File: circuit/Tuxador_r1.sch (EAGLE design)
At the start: 27 parts, among them CN1 MKDSN1,5/2-5,08, CN2 MKDSN1,5/2-5,08, CN3 MKDSN1,5/2-5,08, CN4 MKDSN1,5/2-5,08, IC1 7805T, U1 ATMEGA328P-AU, X1 16MHz

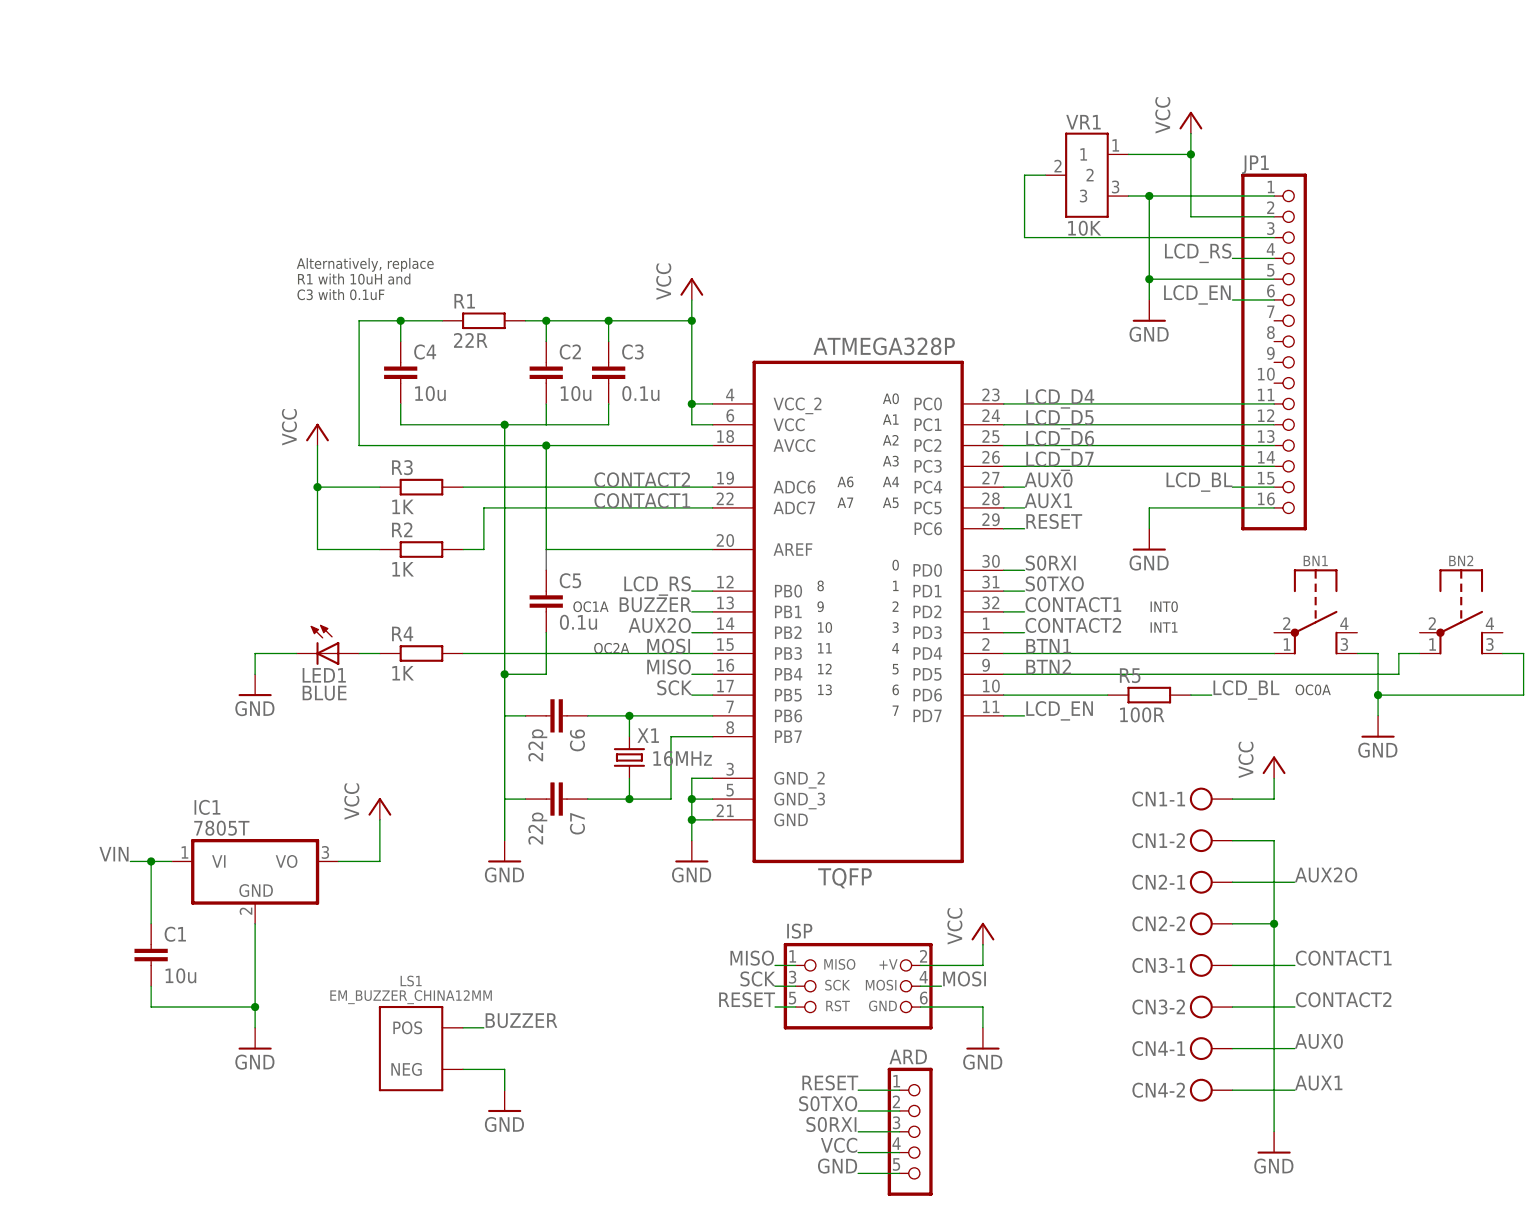
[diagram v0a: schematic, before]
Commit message: Add clamping diodes
Clamping diodes have been added to the contact inputs.

Support for ST7735-compatible LCDs has been added to the main LCD
header.
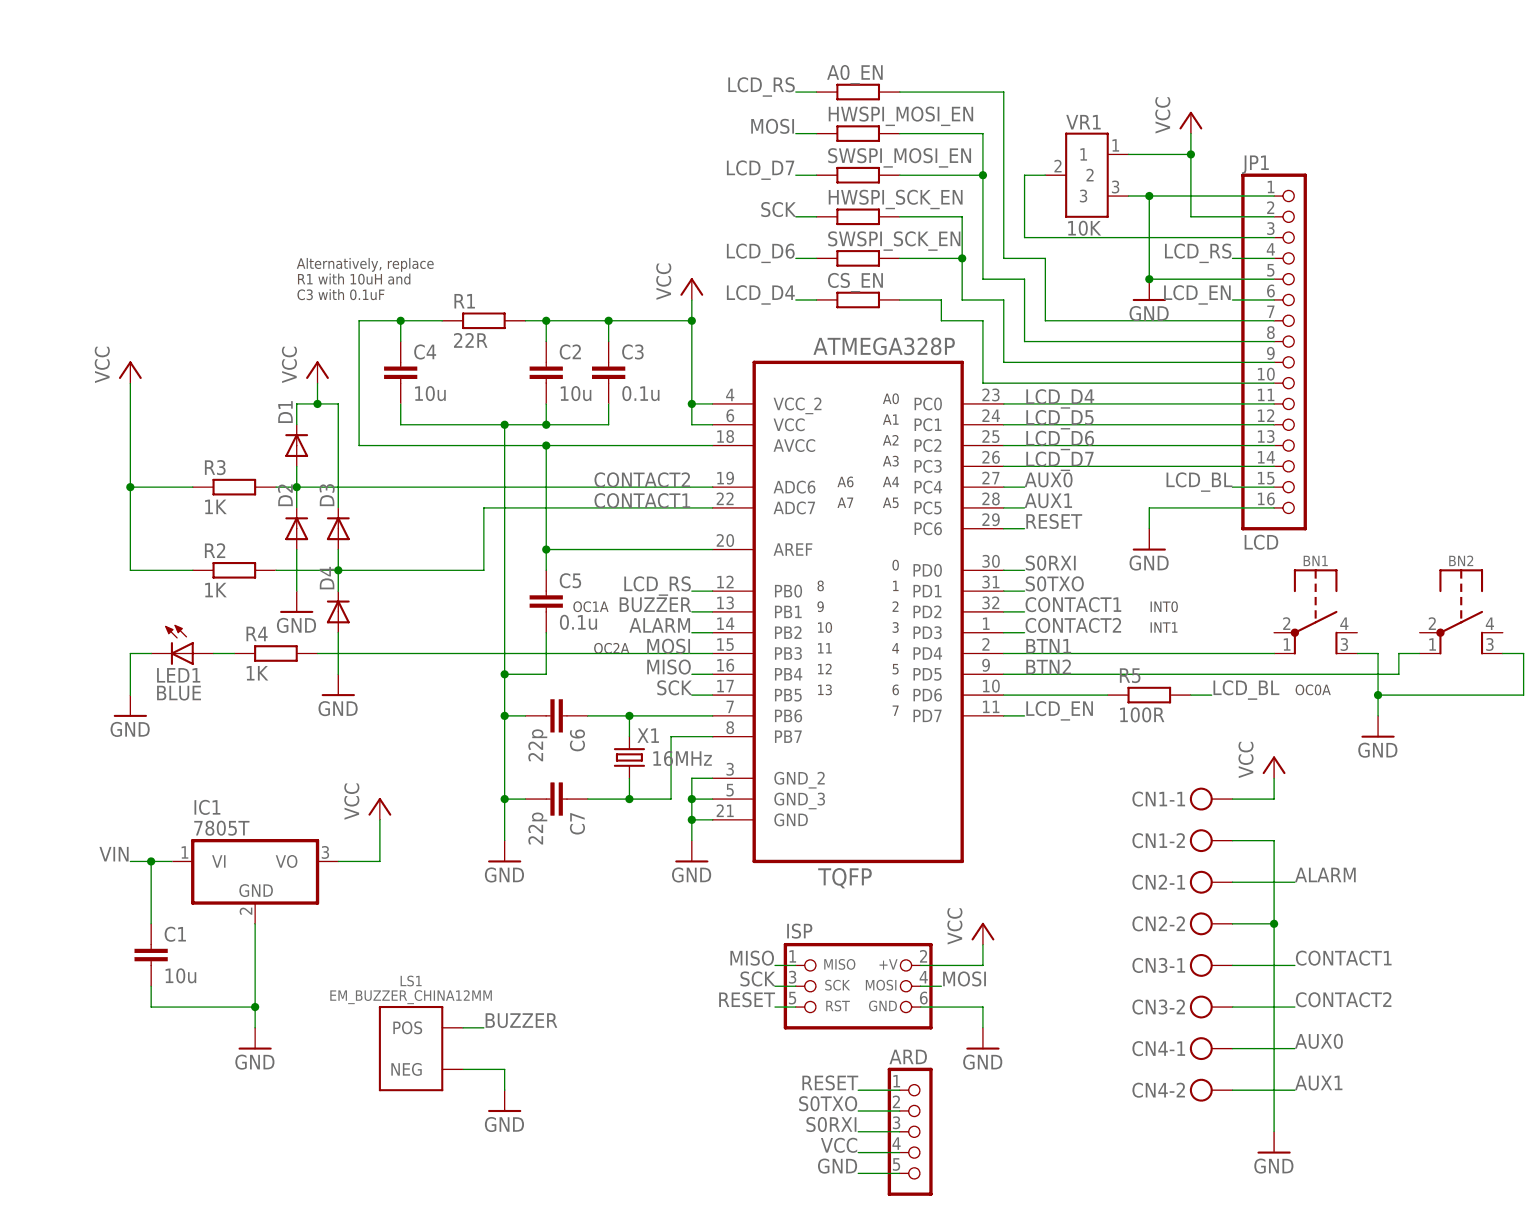
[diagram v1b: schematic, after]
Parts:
- added A0_EN, CS_EN, HWSPI_MOSI_EN, HWSPI_SCK_EN, SWSPI_MOSI_EN, SWSPI_SCK_EN: -0-, rcl:R-EU_R1206
- added D1, D2, D3, D4: (no value), dp_devices:DIODE-SOT23
- JP1: value (none) -> LCD
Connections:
- net AUX2O renamed ALARM
- removed net N$1: C4.1, R1.1, U1.AREF, U1.AVCC
- new net AVCC: C4.1, C5.1, R1.1, U1.AREF, U1.AVCC
- new net N$4: A0_EN.2, JP1.7
- new net N$5: HWSPI_MOSI_EN.2, JP1.8, SWSPI_MOSI_EN.2
- new net N$6: HWSPI_SCK_EN.2, JP1.9, SWSPI_SCK_EN.2
- new net N$7: CS_EN.2, JP1.10
- net CONTACT1: now also D3.A, D4.C
- net CONTACT2: now also D1.A, D2.C
- net GND: now also D2.A, D4.A
- net LCD_D4: now also CS_EN.1
- net LCD_D6: now also SWSPI_SCK_EN.1
- net LCD_D7: now also SWSPI_MOSI_EN.1
- net LCD_RS: now also A0_EN.1
- net MOSI: now also HWSPI_MOSI_EN.1
- net SCK: now also HWSPI_SCK_EN.1
- net VCC: now also D1.C, D3.C
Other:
- moved on the sheet: LED1, R2, R3, R4

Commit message: Minor schematic updates
- Cleaned up some sections
- Added more descriptive text
- Indicated drill-through holes for security on programming headers.
These will be located on their own section on the board but depending on
board costs to mill these sections I want to indicate where a drill can
be used.
- Added a series resistor for the A0 line if using ST7735 LCD, otherwise
it won't work :)
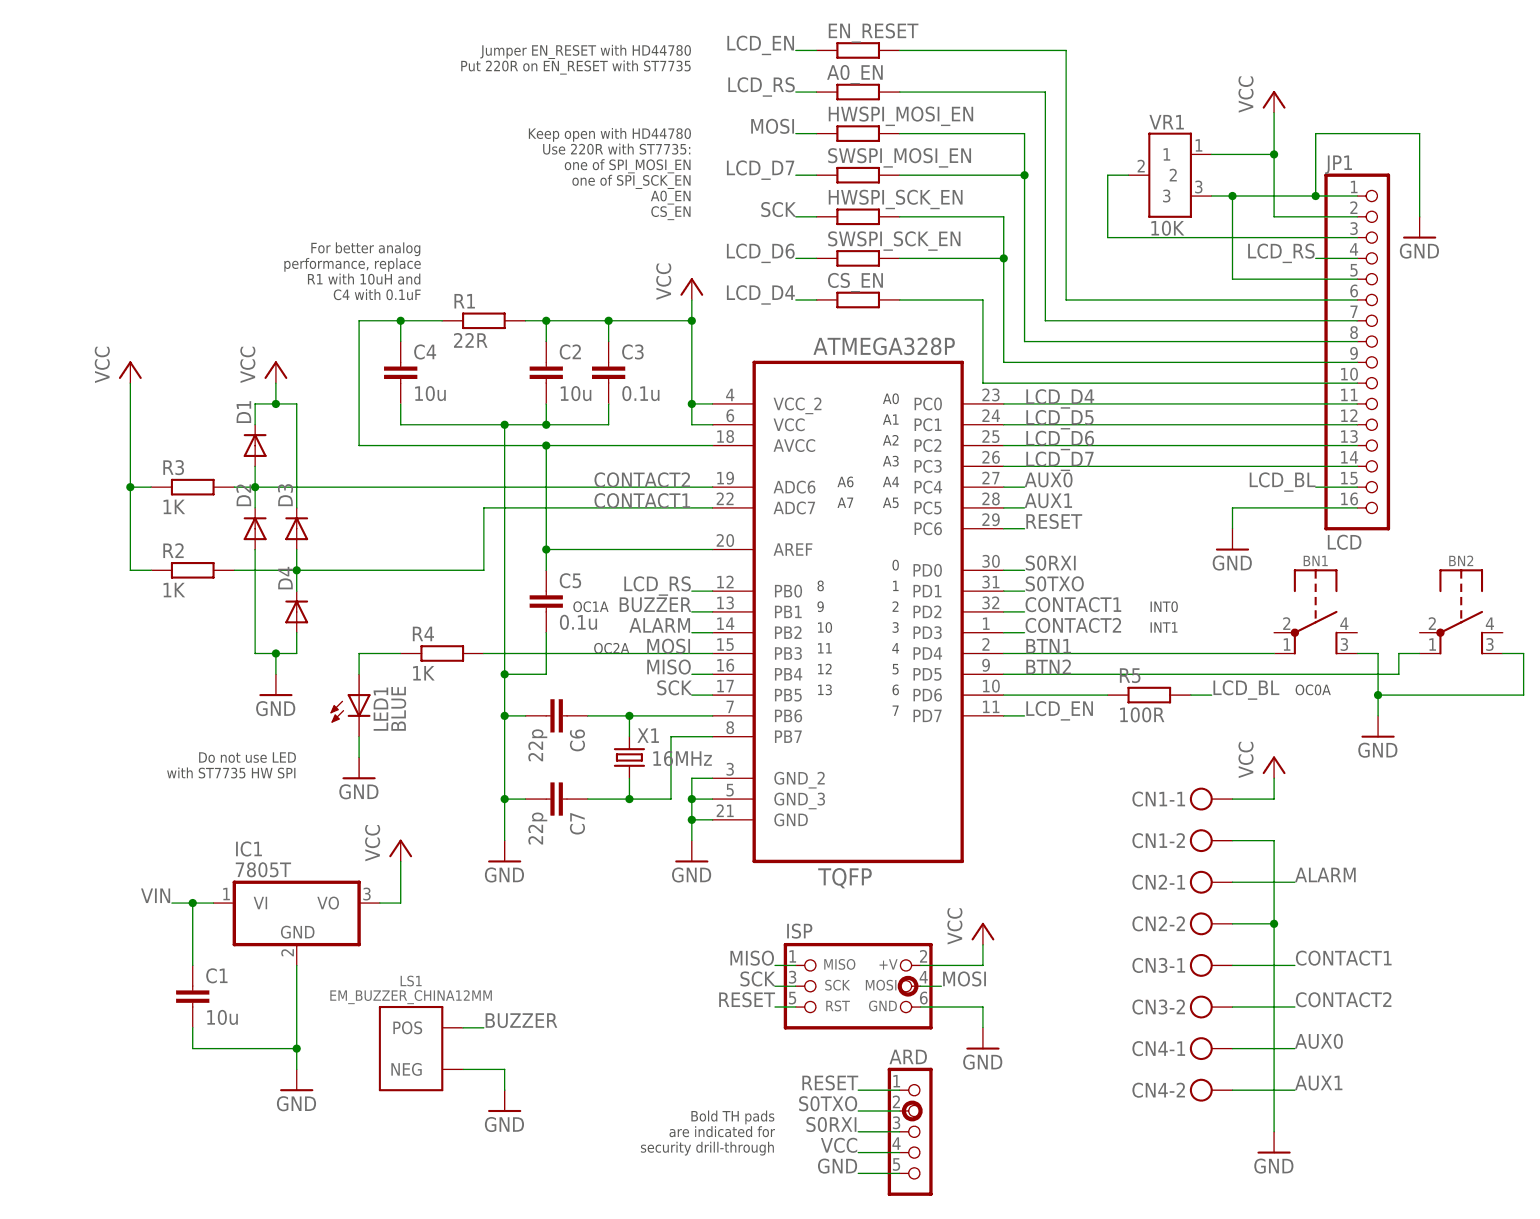
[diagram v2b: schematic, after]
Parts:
- added EN_RESET: -0-, rcl:R-EU_R1206
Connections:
- new net LCD_EN_RESET: EN_RESET.2, JP1.6
- net LCD_EN: now also EN_RESET.1; no longer JP1.6
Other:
- note added: "Bold TH pads are indicated for security drill-through"
- note added: "Do not use LED with ST7735 HW SPI"
- note added: "For better analog performance, replace R1 with 10uH and C4 with 0.1uF"
- note added: "Jumper EN_RESET with HD44780 Put 220R on EN_RESET with ST7735"
- note added: "Keep open with HD44780 Use 220R with ST7735: one of SPI_MOSI_EN one of SPI_SCK_EN A0_EN CS_EN"
- note removed: "Alternatively, replace R1 with 10uH and C3 with 0.1uF"
- moved on the sheet: C1, D1, D2, D3, D4, IC1, JP1, LED1, R2, R3, R4, VR1

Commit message: Added resistors for clamping diode protection
Oops
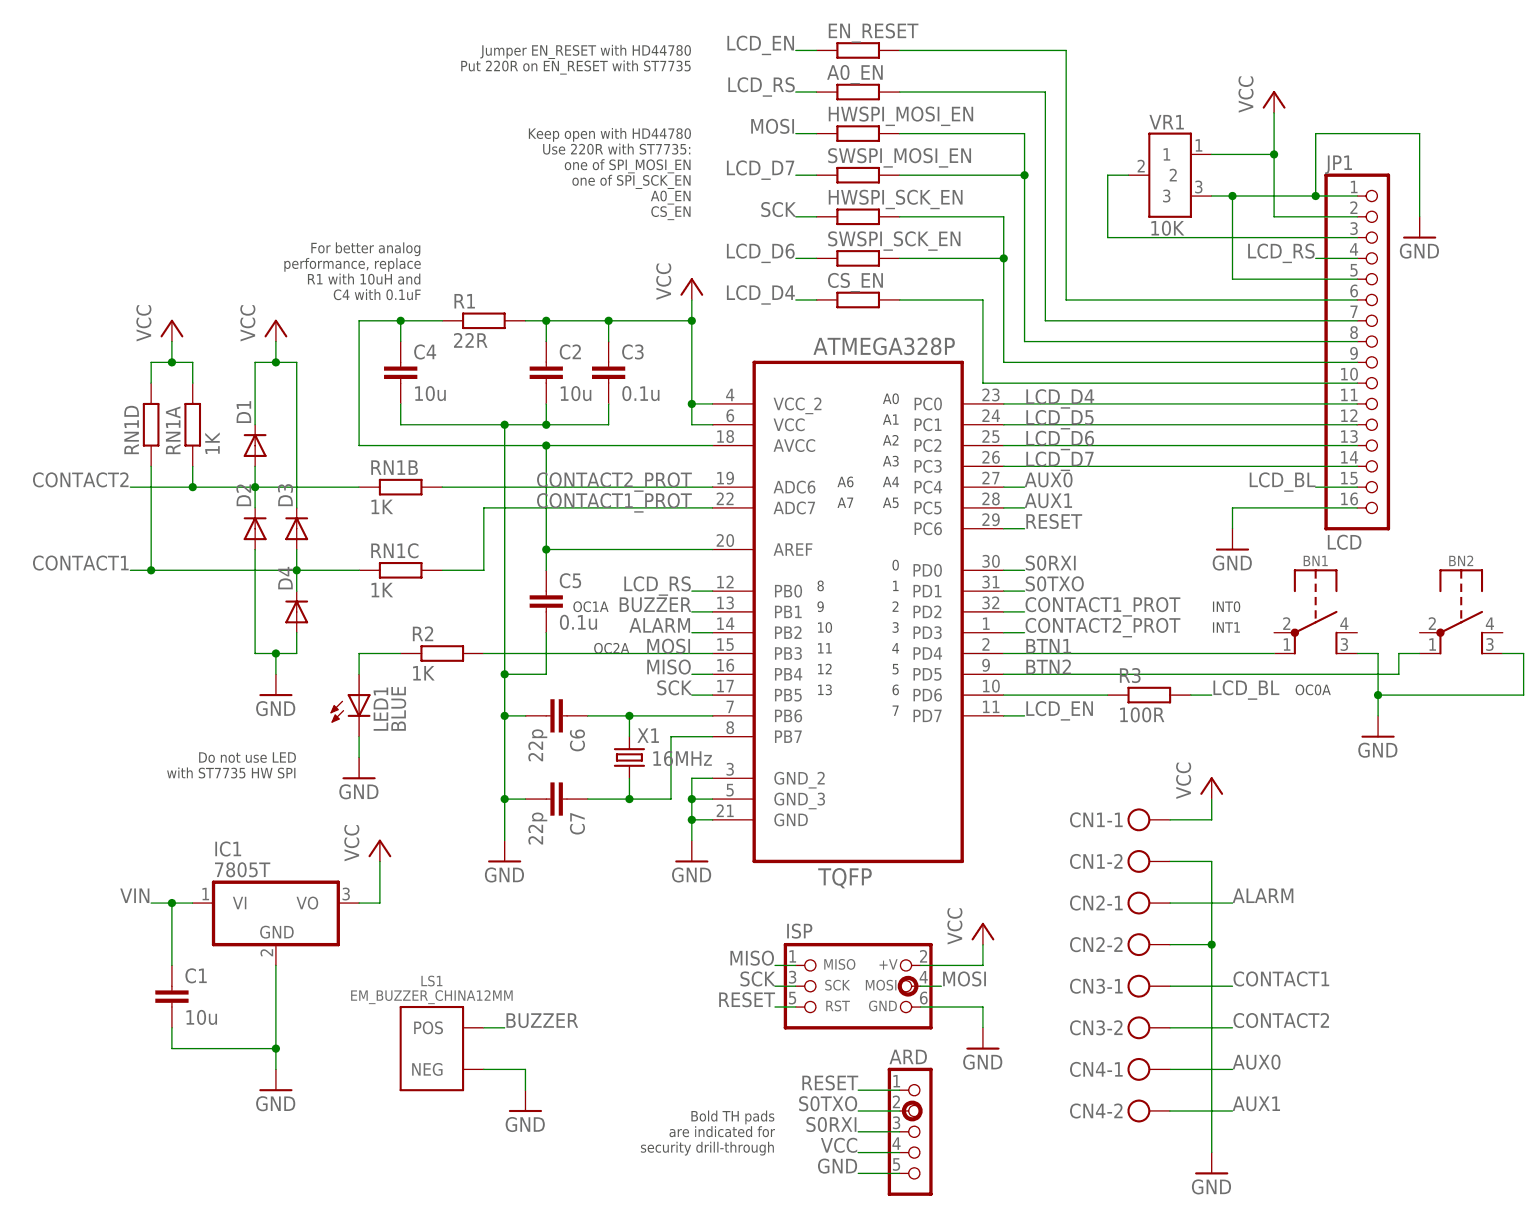
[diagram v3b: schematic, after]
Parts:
- removed R4: 1K, rcl:R-EU_R1206
- removed R5: 100R, rcl:R-EU_R1206
- added RN1: 1K, dp_devices:RESISTOR_ARRAY_4
- R3: value 1K -> 100R
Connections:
- new net CONTACT1_PROT: RN1C.2, U1.ADC7, U1.PD2
- new net CONTACT2_PROT: RN1B.2, U1.ADC6, U1.PD3
- net CONTACT1: now also RN1C.1, RN1D.1; no longer R2.2, U1.ADC7, U1.PD2
- net CONTACT2: now also RN1A.1, RN1B.1; no longer R3.2, U1.ADC6, U1.PD3
- net LCD_BL: now also R3.2; no longer R5.2
- net LCD_BL_MCU: now also R3.1; no longer R5.1
- net MOSI: now also R2.2; no longer R4.2
- net N$1: now also R2.1; no longer R4.1
- net VCC: now also RN1A.2, RN1D.2; no longer R2.1, R3.1
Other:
- moved on the sheet: C1, CN1-1, CN1-2, CN2-1, CN2-2, CN3-1, CN3-2, CN4-1, CN4-2, IC1, LS1, R2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

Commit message: Component update; initial board layout
Components have been updated as necessary for the design. Examples are
changing the voltage regulator and the crystal.

Initial board component placement. Still a lot of work to do here before
running traces.
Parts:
- removed IC1: 7805T, linear:7805T
- added R4: 10K, _trueControl:BI-TECH_36P-POT
- C6, C7: device rcl:C-EUC0805 -> rcl:C-EUC0603
- ISP: value CON_HEADER_PRG_AVR_ICSP -> CON_HEADER_PRG_AVR_ICSP_NOLBL; device dp_devices:CON_HEADER_PRG_AVR_ICSP -> dp_devices:CON_HEADER_PRG_AVR_ICSP_NOLBL
- LED1: device dp_devices:LED-5MM -> dp_devices:LED-3MM
- VR1: value 10K -> LD117AS50TR; device _trueControl:BI-TECH_36P-POT -> v-reg:LD117AS50TR
- X1: value 16MHz -> CRYSTAL-SMD4-3225; device crystal:CRYSTALHC49UP -> abracon:CRYSTAL-SMD4-3225
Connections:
- net ALARM: now also CN2-2.KL; no longer CN2-1.KL
- net CONTACT1: now also CN1-2.KL; no longer CN3-1.KL
- net CONTACT2: now also CN1-1.KL; no longer CN3-2.KL
- net GND: now also CN2-1.KL, CN3-1.KL, R4.3, VR1.ADJ, X1.GND; no longer CN1-2.KL, CN2-2.KL, IC1.GND, VR1.3
- net N$3: now also R4.2; no longer VR1.2
- net OSC1: now also X1.1; no longer X1.2
- net OSC2: now also X1.2; no longer X1.1
- net VCC: now also R4.1, VR1.OUT; no longer CN1-1.KL, IC1.VO, VR1.1
- net VIN: now also CN3-2.KL, VR1.IN; no longer IC1.VI
